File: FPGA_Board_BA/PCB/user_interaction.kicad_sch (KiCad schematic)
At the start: 10 parts, among them SW1201 TL3305BF100QG, SW1202 TL3305BF100QG

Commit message: schematic almost ready pt2
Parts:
- added C901: 100n_0603, WLIB_Capacitor:C_0603, symbol WLIB_C:100n_0603
- added D901, D902: B72590D50H160, Capacitor_SMD:C_0402_1005Metric_Pad0.74x0.62mm_HandSolder, symbol MYLIB_Misc:ESD_Diode_5V6
- added R901: 100R_0603, Resistor_SMD:R_0603_1608Metric, symbol WLIB_R:100R_0603
- added R902: Poti_10k, MYLIB_Misc:RK09D1130A1N, symbol MYLIB_Misc:Potentiometer
- added R903: 100k_0603, Resistor_SMD:R_0603_1608Metric, symbol WLIB_R:100k_0603
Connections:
- net +3.3V: now also R902.1
- net GND: now also C901.2, D901.1 (A1), D902.1 (A1), R902.3, R903.2
- net Poti: now also R901.2
- new net: C901.1, R901.1, R902.2
- new net: D901.2 (A2), D902.2 (A2), R902.4, R902.5, R903.1

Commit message: Besprechung mit Leo
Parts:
- removed D901, D902: B72590D50H160, Capacitor_SMD:C_0402_1005Metric_Pad0.74x0.62mm_HandSolder, symbol MYLIB_Misc:ESD_Diode_5V6
- removed R903: 100k_0603, Resistor_SMD:R_0603_1608Metric, symbol WLIB_R:100k_0603
- added R904, R905: 100R_0603, Resistor_SMD:R_0603_1608Metric, symbol WLIB_R:100R_0603
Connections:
- net Button1: now also R904.2; no longer SW1201.1
- net Button2: now also R905.2; no longer SW1202.1
- net GND: now also R902.4, R902.5
- new net: R905.1, SW1202.1
- new net: R904.1, SW1201.1
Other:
- moved on the sheet: SW1201, SW1202

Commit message: work
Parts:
- renumbered C1201 to C54, C1202 to C55, C901 to C56, D1201 to D7, D1202 to D8, R1202 to R44, R1201 to R45, R904 to R46, R1203 to R47, R905 to R48, R1204 to R49, R902 to R50, R901 to R51, SW1201 to SW1, SW1202 to SW2
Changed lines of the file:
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@@
 		(on_board yes)
 		(dnp no)
-		(property "Reference" "#PWR01204"
+		(property "Reference" "#PWR063"
 			(at 154.94 167.64 0)
 			(effects
@@
 			(project "FPGA_Board_BA"
 				(path "/fd7503bc-e7fc-4766-b224-3d1c3d7de5ff/4cefeee2-fd60-4f1a-a208-06a5d0a2f90a"
-					(reference "#PWR01204")
+					(reference "#PWR063")
 					(unit 1)
 				)
@@
 		(dnp no)
 		(fields_autoplaced yes)
-		(property "Reference" "#PWR01202"
+		(property "Reference" "#PWR062"
 			(at 133.35 109.22 0)
 			(effects
@@
 			(project ""
 				(path "/fd7503bc-e7fc-4766-b224-3d1c3d7de5ff/4cefeee2-fd60-4f1a-a208-06a5d0a2f90a"
-					(reference "#PWR01202")
+					(reference "#PWR062")
 					(unit 1)
 				)
@@
 		(on_board yes)
 		(dnp no)
-		(property "Reference" "R1204"
+		(property "Reference" "R49"
 			(at 161.036 150.622 90)
 			(effects
@@
 			(project "FPGA_Board_BA"
 				(path "/fd7503bc-e7fc-4766-b224-3d1c3d7de5ff/4cefeee2-fd60-4f1a-a208-06a5d0a2f90a"
-					(reference "R1204")
+					(reference "R49")
 					(unit 1)
 				)
@@
 		(dnp no)
 		(fields_autoplaced yes)
-		(property "Reference" "C1201"
+		(property "Reference" "C54"
 			(at 143.51 146.0499 0)
 			(effects
@@
 			(project ""
 				(path "/fd7503bc-e7fc-4766-b224-3d1c3d7de5ff/4cefeee2-fd60-4f1a-a208-06a5d0a2f90a"
-					(reference "C1201")
+					(reference "C54")
 					(unit 1)
 				)
@@
 		(dnp no)
 		(fields_autoplaced yes)
-		(property "Reference" "R902"
+		(property "Reference" "R50"
 			(at 186.69 66.0399 0)
 			(effects
@@
 			(project ""
 				(path "/fd7503bc-e7fc-4766-b224-3d1c3d7de5ff/4cefeee2-fd60-4f1a-a208-06a5d0a2f90a"
-					(reference "R902")
+					(reference "R50")
 					(unit 1)
 				)
@@
 		(dnp no)
 		(fields_autoplaced yes)
-		(property "Reference" "#PWR0903"
+		(property "Reference" "#PWR065"
 			(at 191.77 58.42 0)
 			(effects
@@
 			(project "FPGA_Board_BA"
 				(path "/fd7503bc-e7fc-4766-b224-3d1c3d7de5ff/4cefeee2-fd60-4f1a-a208-06a5d0a2f90a"
-					(reference "#PWR0903")
+					(reference "#PWR065")
 					(unit 1)
 				)
@@
 		(dnp no)
 		(fields_autoplaced yes)
-		(property "Reference" "R1201"
+		(property "Reference" "R45"
 			(at 80.01 102.8699 0)
 			(effects
@@
 			(project ""
 				(path "/fd7503bc-e7fc-4766-b224-3d1c3d7de5ff/4cefeee2-fd60-4f1a-a208-06a5d0a2f90a"
-					(reference "R1201")
+					(reference "R45")
 					(unit 1)
 				)
@@
 		(on_board yes)
 		(dnp no)
-		(property "Reference" "SW1202"
+		(property "Reference" "SW2"
 			(at 159.258 124.714 0)
 			(effects
@@
 			(project "FPGA_Board_BA"
 				(path "/fd7503bc-e7fc-4766-b224-3d1c3d7de5ff/4cefeee2-fd60-4f1a-a208-06a5d0a2f90a"
-					(reference "SW1202")
+					(reference "SW2")
 					(unit 1)
 				)
@@
 		(dnp no)
 		(fields_autoplaced yes)
-		(property "Reference" "#PWR01201"
+		(property "Reference" "#PWR061"
 			(at 67.31 140.97 0)
 			(effects
@@
 			(project ""
 				(path "/fd7503bc-e7fc-4766-b224-3d1c3d7de5ff/4cefeee2-fd60-4f1a-a208-06a5d0a2f90a"
-					(reference "#PWR01201")
+					(reference "#PWR061")
 					(unit 1)
 				)
@@
 		(on_board yes)
 		(dnp no)
-		(property "Reference" "SW1201"
+		(property "Reference" "SW1"
 			(at 125.984 123.952 0)
 			(effects
@@
 			(project ""
 				(path "/fd7503bc-e7fc-4766-b224-3d1c3d7de5ff/4cefeee2-fd60-4f1a-a208-06a5d0a2f90a"
-					(reference "SW1201")
+					(reference "SW1")
 					(unit 1)
 				)
@@
 		(on_board yes)
 		(dnp no)
-		(property "Reference" "#PWR0902"
+		(property "Reference" "#PWR066"
 			(at 219.71 104.14 0)
 			(effects
@@
 			(project "FPGA_Board_BA"
 				(path "/fd7503bc-e7fc-4766-b224-3d1c3d7de5ff/4cefeee2-fd60-4f1a-a208-06a5d0a2f90a"
-					(reference "#PWR0902")
+					(reference "#PWR066")
 					(unit 1)
 				)
@@
 		(dnp no)
 		(fields_autoplaced yes)
-		(property "Reference" "R904"
+		(property "Reference" "R46"
 			(at 135.89 128.2699 0)
 			(effects
@@
 			(project ""
 				(path "/fd7503bc-e7fc-4766-b224-3d1c3d7de5ff/4cefeee2-fd60-4f1a-a208-06a5d0a2f90a"
-					(reference "R904")
+					(reference "R46")
 					(unit 1)
 				)
@@
 		(dnp no)
 		(fields_autoplaced yes)
-		(property "Reference" "R901"
+		(property "Reference" "R51"
 			(at 243.84 60.96 90)
 			(effects
@@
 			(project ""
 				(path "/fd7503bc-e7fc-4766-b224-3d1c3d7de5ff/4cefeee2-fd60-4f1a-a208-06a5d0a2f90a"
-					(reference "R901")
+					(reference "R51")
 					(unit 1)
 				)
@@
 		(dnp no)
 		(fields_autoplaced yes)
-		(property "Reference" "R1202"
+		(property "Reference" "R44"
 			(at 60.96 102.8699 0)
 			(effects
@@
 			(project "FPGA_Board_BA"
 				(path "/fd7503bc-e7fc-4766-b224-3d1c3d7de5ff/4cefeee2-fd60-4f1a-a208-06a5d0a2f90a"
-					(reference "R1202")
+					(reference "R44")
 					(unit 1)
 				)
@@
 		(dnp no)
 		(fields_autoplaced yes)
-		(property "Reference" "D1202"
+		(property "Reference" "D8"
 			(at 81.28 120.9674 90)
 			(effects
@@
 			(project ""
 				(path "/fd7503bc-e7fc-4766-b224-3d1c3d7de5ff/4cefeee2-fd60-4f1a-a208-06a5d0a2f90a"
-					(reference "D1202")
+					(reference "D8")
 					(unit 1)
 				)
@@
 		(dnp no)
 		(fields_autoplaced yes)
-		(property "Reference" "R905"
+		(property "Reference" "R48"
 			(at 168.91 128.2699 0)
 			(effects
@@
 			(project "FPGA_Board_BA"
 				(path "/fd7503bc-e7fc-4766-b224-3d1c3d7de5ff/4cefeee2-fd60-4f1a-a208-06a5d0a2f90a"
-					(reference "R905")
+					(reference "R48")
 					(unit 1)
 				)
@@
 		(on_board yes)
 		(dnp no)
-		(property "Reference" "R1203"
+		(property "Reference" "R47"
 			(at 127.508 151.892 90)
 			(effects
@@
 			(project ""
 				(path "/fd7503bc-e7fc-4766-b224-3d1c3d7de5ff/4cefeee2-fd60-4f1a-a208-06a5d0a2f90a"
-					(reference "R1203")
+					(reference "R47")
 					(unit 1)
 				)
@@
 		(dnp no)
 		(fields_autoplaced yes)
-		(property "Reference" "C901"
+		(property "Reference" "C56"
 			(at 238.76 78.7399 0)
 			(effects
@@
 			(project "FPGA_Board_BA"
 				(path "/fd7503bc-e7fc-4766-b224-3d1c3d7de5ff/4cefeee2-fd60-4f1a-a208-06a5d0a2f90a"
-					(reference "C901")
+					(reference "C56")
 					(unit 1)
 				)
@@
 		(dnp no)
 		(fields_autoplaced yes)
-		(property "Reference" "C1202"
+		(property "Reference" "C55"
 			(at 176.53 144.7799 0)
 			(effects
@@
 			(project "FPGA_Board_BA"
 				(path "/fd7503bc-e7fc-4766-b224-3d1c3d7de5ff/4cefeee2-fd60-4f1a-a208-06a5d0a2f90a"
-					(reference "C1202")
+					(reference "C55")
 					(unit 1)
 				)
@@
 		(dnp no)
 		(fields_autoplaced yes)
-		(property "Reference" "#PWR01203"
+		(property "Reference" "#PWR064"
 			(at 166.37 109.22 0)
 			(effects
@@
 			(project "FPGA_Board_BA"
 				(path "/fd7503bc-e7fc-4766-b224-3d1c3d7de5ff/4cefeee2-fd60-4f1a-a208-06a5d0a2f90a"
-					(reference "#PWR01203")
+					(reference "#PWR064")
 					(unit 1)
 				)
@@
 		(dnp no)
 		(fields_autoplaced yes)
-		(property "Reference" "D1201"
+		(property "Reference" "D7"
 			(at 62.23 120.9674 90)
 			(effects
@@
 			(project ""
 				(path "/fd7503bc-e7fc-4766-b224-3d1c3d7de5ff/4cefeee2-fd60-4f1a-a208-06a5d0a2f90a"
-					(reference "D1201")
-					(unit 1)
-				)
+					(reference "D7")
+					(unit 1)
+				)

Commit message: 18.11 Bib Session
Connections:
- net +3.3V: no longer R50.1
- new net +1V8: R50.1

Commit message: Besprechung mit Leo
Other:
- note added: "Poti -> ADC of B6 Vmax: 4.096V"
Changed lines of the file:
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@@
 	(generator_version "9.0")
 	(paper "A4")
+	(text "Poti -> ADC of B6\nVmax: 4.096V"
+		(exclude_from_sim no)
+		(at 216.916 57.912 0)
+		(effects
+			(font
+				(size 1.27 1.27)
+			)
+		)
+	)
 	(junction
 		(at 133.35 139.7)

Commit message: 22.11
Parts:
- removed D7: LED_B_0603, WLIB_DO:LED_0603_1608Metric, symbol WLIB_D:LED_B_0603
- removed D8: LED_G_0603, WLIB_DO:LED_0603_1608Metric, symbol WLIB_D:LED_G_0603
- added C57: 100n_0603, WLIB_Capacitor:C_0603, symbol WLIB_C:100n_0603
- added D11: LED_B_0603, LED_SMD:LED_0603_1608Metric, symbol WLIB_D:LED_B_0603
- added D12: LED_G_0603, LED_SMD:LED_0603_1608Metric, symbol WLIB_D:LED_G_0603
- added D13: LED_R_0603, LED_SMD:LED_0603_1608Metric, symbol WLIB_D:LED_R_0603
- added R39, R40, R41, R43, R49, R50, R52: 10k_0603, Resistor_SMD:R_0603_1608Metric, symbol WLIB_R:10k_0603
- added R51: Poti_10k, MYLIB_Misc:RK09D1130A1N, symbol MYLIB_Misc:Potentiometer
- added R53: 100R_0603, Resistor_SMD:R_0603_1608Metric, symbol WLIB_R:100R_0603
- renumbered C56 to C54, C54 to C55, C55 to C56, R44 to R37, R45 to R38, R50 to R42, R46 to R44, R47 to R45, R51 to R46, R48 to R47, R49 to R48
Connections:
- net +3.3V: now also SW1.3, SW1.4, SW2.3, SW2.4; no longer SW1.2, SW2.2
- net GND: now also C57.2, D11.1 (K), D12.1 (K), D13.1 (K), R51.3, R51.4, R51.5
- net at R38.2: now also D12.2 (A)
- net at R47.1, SW2.1: now also SW2.2
- net at R44.1, SW1.1: now also SW1.2
- net at R37.2: now also D11.2 (A)
- net +1V8: no longer names the net of R42.1
- net +1V8: now also R40.2, R41.2, R43.2
- new net: C57.1, R51.2, R53.1
- new net: R49.2, R50.2, R51.1, R52.2
- new net: D13.2 (A), R39.2
- new net +5VA: R40.1, R41.1, R43.1, R49.1, R50.1, R52.1
- new net LED3: R39.1
- new net Poti2: R53.2
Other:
- note added: "Poti -> XADC (Vref = 1.25V) Vout = Vin * R1 / (R1 + R2) 1.25/5 = R1/(R1+10k) 0.25*(R1 + 10k) = R1 0.75*R1 = 2.5k R1 = 2.5k/0.75 = 3k33"
- note removed: "Poti -> ADC of B6 Vmax: 4.096V"
- moved on the sheet: C54, C55, C56, R37, R38, R42, R44, R45, R46, R47, R48

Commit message: exported stuff
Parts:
- renumbered R37 to R49, R38 to R50, R39 to R51, R40 to R52, R41 to R53, R42 to R54, R43 to R55, R44 to R56, R45 to R57, R46 to R58, R47 to R59, R48 to R60, R49 to R61, R50 to R62, R51 to R63, R52 to R64, R53 to R65
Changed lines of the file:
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@@
 		(on_board yes)
 		(dnp no)
-		(property "Reference" "#PWR070"
+		(property "Reference" "#PWR075"
 			(at 139.7 187.96 0)
 			(effects
@@
 			(project "FPGA_Board_BA"
 				(path "/fd7503bc-e7fc-4766-b224-3d1c3d7de5ff/4cefeee2-fd60-4f1a-a208-06a5d0a2f90a"
-					(reference "#PWR070")
+					(reference "#PWR075")
 					(unit 1)
 				)
@@
 		(dnp no)
 		(fields_autoplaced yes)
-		(property "Reference" "#PWR072"
+		(property "Reference" "#PWR077"
 			(at 167.64 29.21 0)
 			(effects
@@
 			(project "FPGA_Board_BA"
 				(path "/fd7503bc-e7fc-4766-b224-3d1c3d7de5ff/4cefeee2-fd60-4f1a-a208-06a5d0a2f90a"
-					(reference "#PWR072")
+					(reference "#PWR077")
 					(unit 1)
 				)
@@
 		(dnp no)
 		(fields_autoplaced yes)
-		(property "Reference" "#PWR069"
+		(property "Reference" "#PWR074"
 			(at 118.11 129.54 0)
 			(effects
@@
 			(project ""
 				(path "/fd7503bc-e7fc-4766-b224-3d1c3d7de5ff/4cefeee2-fd60-4f1a-a208-06a5d0a2f90a"
-					(reference "#PWR069")
-					(unit 1)
-				)
-			)
-		)
-	)
-	(symbol
-		(lib_name "LED_B_0603_1")
+					(reference "#PWR074")
+					(unit 1)
+				)
+			)
+		)
+	)
+	(symbol
 		(lib_id "WLIB_D:LED_B_0603")
 		(at 26.67 158.75 90)
@@
 		(on_board yes)
 		(dnp no)
-		(property "Reference" "R48"
+		(property "Reference" "R60"
 			(at 145.796 170.942 90)
 			(effects
@@
 			(project "FPGA_Board_BA"
 				(path "/fd7503bc-e7fc-4766-b224-3d1c3d7de5ff/4cefeee2-fd60-4f1a-a208-06a5d0a2f90a"
-					(reference "R48")
+					(reference "R60")
 					(unit 1)
 				)
@@
 		(on_board yes)
 		(dnp no)
-		(property "Reference" "R43"
+		(property "Reference" "R55"
 			(at 97.536 43.942 90)
 			(effects
@@
 			(project "FPGA_Board_BA"
 				(path "/fd7503bc-e7fc-4766-b224-3d1c3d7de5ff/4cefeee2-fd60-4f1a-a208-06a5d0a2f90a"
-					(reference "R43")
+					(reference "R55")
 					(unit 1)
 				)
@@
 		(dnp no)
 		(fields_autoplaced yes)
-		(property "Reference" "#PWR067"
+		(property "Reference" "#PWR072"
 			(at 93.98 29.21 0)
 			(effects
@@
 			(project ""
 				(path "/fd7503bc-e7fc-4766-b224-3d1c3d7de5ff/4cefeee2-fd60-4f1a-a208-06a5d0a2f90a"
-					(reference "#PWR067")
+					(reference "#PWR072")
 					(unit 1)
 				)
@@
 		(on_board yes)
 		(dnp no)
-		(property "Reference" "#PWR073"
+		(property "Reference" "#PWR078"
 			(at 179.07 100.33 0)
 			(effects
@@
 			(project "FPGA_Board_BA"
 				(path "/fd7503bc-e7fc-4766-b224-3d1c3d7de5ff/4cefeee2-fd60-4f1a-a208-06a5d0a2f90a"
-					(reference "#PWR073")
+					(reference "#PWR078")
 					(unit 1)
 				)
@@
 		(dnp no)
 		(fields_autoplaced yes)
-		(property "Reference" "R42"
+		(property "Reference" "R54"
 			(at 88.9 60.9599 0)
 			(effects
@@
 			(project ""
 				(path "/fd7503bc-e7fc-4766-b224-3d1c3d7de5ff/4cefeee2-fd60-4f1a-a208-06a5d0a2f90a"
-					(reference "R42")
+					(reference "R54")
 					(unit 1)
 				)
@@
 		(dnp no)
 		(fields_autoplaced yes)
-		(property "Reference" "R53"
+		(property "Reference" "R65"
 			(at 198.12 55.88 90)
 			(effects
@@
 			(project "FPGA_Board_BA"
 				(path "/fd7503bc-e7fc-4766-b224-3d1c3d7de5ff/4cefeee2-fd60-4f1a-a208-06a5d0a2f90a"
-					(reference "R53")
+					(reference "R65")
 					(unit 1)
 				)
@@
 		(dnp no)
 		(fields_autoplaced yes)
-		(property "Reference" "R38"
+		(property "Reference" "R50"
 			(at 48.26 143.5099 0)
 			(effects
@@
 			(project ""
 				(path "/fd7503bc-e7fc-4766-b224-3d1c3d7de5ff/4cefeee2-fd60-4f1a-a208-06a5d0a2f90a"
-					(reference "R38")
+					(reference "R50")
 					(unit 1)
 				)
@@
 		(on_board yes)
 		(dnp no)
-		(property "Reference" "R40"
+		(property "Reference" "R52"
 			(at 79.756 43.942 90)
 			(effects
@@
 			(project ""
 				(path "/fd7503bc-e7fc-4766-b224-3d1c3d7de5ff/4cefeee2-fd60-4f1a-a208-06a5d0a2f90a"
-					(reference "R40")
+					(reference "R52")
 					(unit 1)
 				)
@@
 		(dnp no)
 		(fields_autoplaced yes)
-		(property "Reference" "#PWR066"
+		(property "Reference" "#PWR071"
 			(at 35.56 179.07 0)
 			(effects
@@
 			(project ""
 				(path "/fd7503bc-e7fc-4766-b224-3d1c3d7de5ff/4cefeee2-fd60-4f1a-a208-06a5d0a2f90a"
-					(reference "#PWR066")
+					(reference "#PWR071")
 					(unit 1)
 				)
@@
 		(on_board yes)
 		(dnp no)
-		(property "Reference" "R50"
+		(property "Reference" "R62"
 			(at 162.306 43.942 90)
 			(effects
@@
 			(project "FPGA_Board_BA"
 				(path "/fd7503bc-e7fc-4766-b224-3d1c3d7de5ff/4cefeee2-fd60-4f1a-a208-06a5d0a2f90a"
-					(reference "R50")
+					(reference "R62")
 					(unit 1)
 				)
@@
 		(on_board yes)
 		(dnp no)
-		(property "Reference" "R41"
+		(property "Reference" "R53"
 			(at 88.646 43.942 90)
 			(effects
@@
 			(project "FPGA_Board_BA"
 				(path "/fd7503bc-e7fc-4766-b224-3d1c3d7de5ff/4cefeee2-fd60-4f1a-a208-06a5d0a2f90a"
-					(reference "R41")
+					(reference "R53")
 					(unit 1)
 				)
@@
 		(on_board yes)
 		(dnp no)
-		(property "Reference" "R52"
+		(property "Reference" "R64"
 			(at 171.196 43.942 90)
 			(effects
@@
 			(project "FPGA_Board_BA"
 				(path "/fd7503bc-e7fc-4766-b224-3d1c3d7de5ff/4cefeee2-fd60-4f1a-a208-06a5d0a2f90a"
-					(reference "R52")
+					(reference "R64")
 					(unit 1)
 				)
@@
 		(on_board yes)
 		(dnp no)
-		(property "Reference" "#PWR068"
+		(property "Reference" "#PWR073"
 			(at 105.41 100.33 0)
 			(effects
@@
 			(project "FPGA_Board_BA"
 				(path "/fd7503bc-e7fc-4766-b224-3d1c3d7de5ff/4cefeee2-fd60-4f1a-a208-06a5d0a2f90a"
-					(reference "#PWR068")
+					(reference "#PWR073")
 					(unit 1)
 				)
@@
 		(dnp no)
 		(fields_autoplaced yes)
-		(property "Reference" "R44"
+		(property "Reference" "R56"
 			(at 120.65 148.5899 0)
 			(effects
@@
 			(project ""
 				(path "/fd7503bc-e7fc-4766-b224-3d1c3d7de5ff/4cefeee2-fd60-4f1a-a208-06a5d0a2f90a"
-					(reference "R44")
+					(reference "R56")
 					(unit 1)
 				)
@@
 		(dnp no)
 		(fields_autoplaced yes)
-		(property "Reference" "R46"
+		(property "Reference" "R58"
 			(at 124.46 55.88 90)
 			(effects
@@
 			(project ""
 				(path "/fd7503bc-e7fc-4766-b224-3d1c3d7de5ff/4cefeee2-fd60-4f1a-a208-06a5d0a2f90a"
-					(reference "R46")
+					(reference "R58")
 					(unit 1)
 				)
@@
 		(dnp no)
 		(fields_autoplaced yes)
-		(property "Reference" "R37"
+		(property "Reference" "R49"
 			(at 29.21 143.5099 0)
 			(effects
@@
 			(project "FPGA_Board_BA"
 				(path "/fd7503bc-e7fc-4766-b224-3d1c3d7de5ff/4cefeee2-fd60-4f1a-a208-06a5d0a2f90a"
-					(reference "R37")
-					(unit 1)
-				)
-			)
-		)
-	)
-	(symbol
-		(lib_name "LED_G_0603_1")
+					(reference "R49")
+					(unit 1)
+				)
+			)
+		)
+	)
+	(symbol
 		(lib_id "WLIB_D:LED_G_0603")
 		(at 45.72 158.75 90)
@@
 		(dnp no)
 		(fields_autoplaced yes)
-		(property "Reference" "R47"
+		(property "Reference" "R59"
 			(at 153.67 148.5899 0)
 			(effects
@@
 			(project "FPGA_Board_BA"
 				(path "/fd7503bc-e7fc-4766-b224-3d1c3d7de5ff/4cefeee2-fd60-4f1a-a208-06a5d0a2f90a"
-					(reference "R47")
+					(reference "R59")
 					(unit 1)
 				)
@@
 		(on_board yes)
 		(dnp no)
-		(property "Reference" "R45"
+		(property "Reference" "R57"
 			(at 112.268 172.212 90)
 			(effects
@@
 			(project ""
 				(path "/fd7503bc-e7fc-4766-b224-3d1c3d7de5ff/4cefeee2-fd60-4f1a-a208-06a5d0a2f90a"
-					(reference "R45")
+					(reference "R57")
 					(unit 1)
 				)
@@
 		(dnp no)
 		(fields_autoplaced yes)
-		(property "Reference" "#PWR071"
+		(property "Reference" "#PWR076"
 			(at 151.13 129.54 0)
 			(effects
@@
 			(project "FPGA_Board_BA"
 				(path "/fd7503bc-e7fc-4766-b224-3d1c3d7de5ff/4cefeee2-fd60-4f1a-a208-06a5d0a2f90a"
-					(reference "#PWR071")
+					(reference "#PWR076")
 					(unit 1)
 				)
@@
 		(on_board yes)
 		(dnp no)
-		(property "Reference" "R49"
+		(property "Reference" "R61"
 			(at 153.416 43.942 90)
 			(effects
@@
 			(project "FPGA_Board_BA"
 				(path "/fd7503bc-e7fc-4766-b224-3d1c3d7de5ff/4cefeee2-fd60-4f1a-a208-06a5d0a2f90a"
-					(reference "R49")
+					(reference "R61")
 					(unit 1)
 				)
@@
 		(dnp no)
 		(fields_autoplaced yes)
-		(property "Reference" "R51"
+		(property "Reference" "R63"
 			(at 162.56 60.9599 0)
 			(effects
@@
 			(project "FPGA_Board_BA"
 				(path "/fd7503bc-e7fc-4766-b224-3d1c3d7de5ff/4cefeee2-fd60-4f1a-a208-06a5d0a2f90a"
-					(reference "R51")
+					(reference "R63")
 					(unit 1)
 				)
@@
 		(dnp no)
 		(fields_autoplaced yes)
-		(property "Reference" "R39"
+		(property "Reference" "R51"
 			(at 71.12 143.5099 0)
 			(effects
@@
 			(project "FPGA_Board_BA"
 				(path "/fd7503bc-e7fc-4766-b224-3d1c3d7de5ff/4cefeee2-fd60-4f1a-a208-06a5d0a2f90a"
-					(reference "R39")
-					(unit 1)
-				)
+					(reference "R51")
+					(unit 1)
+				)

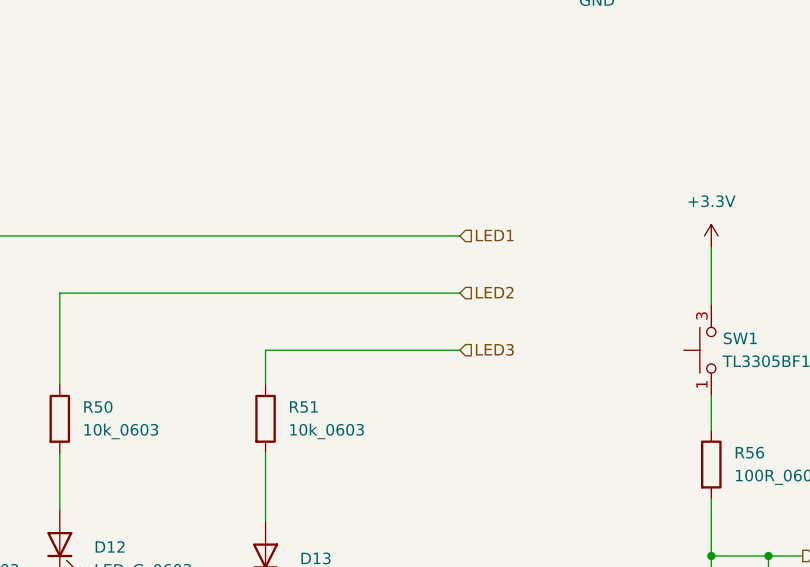
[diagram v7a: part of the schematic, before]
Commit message: big schematic cleanup. Added wire to bus
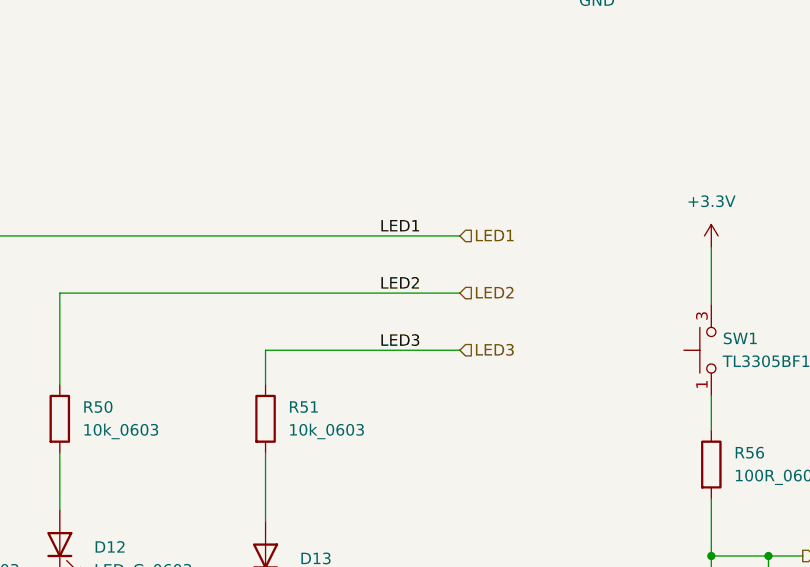
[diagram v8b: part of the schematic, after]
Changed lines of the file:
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@@
+		)
+	)
+	(label "LED3"
+		(at 81.28 137.16 0)
+		(effects
+			(font
+				(size 1.27 1.27)
+			)
+			(justify left bottom)
+		)
+	)
+	(label "LED2"
+		(at 81.28 130.81 0)
+		(effects
+			(font
+				(size 1.27 1.27)
+			)
+			(justify left bottom)
+		)
+	)
+	(label "LED1"
+		(at 81.28 124.46 0)
+		(effects
+			(font
+				(size 1.27 1.27)
+			)
+			(justify left bottom)
 		)
 	)
